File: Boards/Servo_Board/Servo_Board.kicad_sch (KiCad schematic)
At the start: 16 parts, among them U1 STM32G0B1RCTx, U2 ADP2302ARDZ-5.0, Y2 Crystal 8MHz

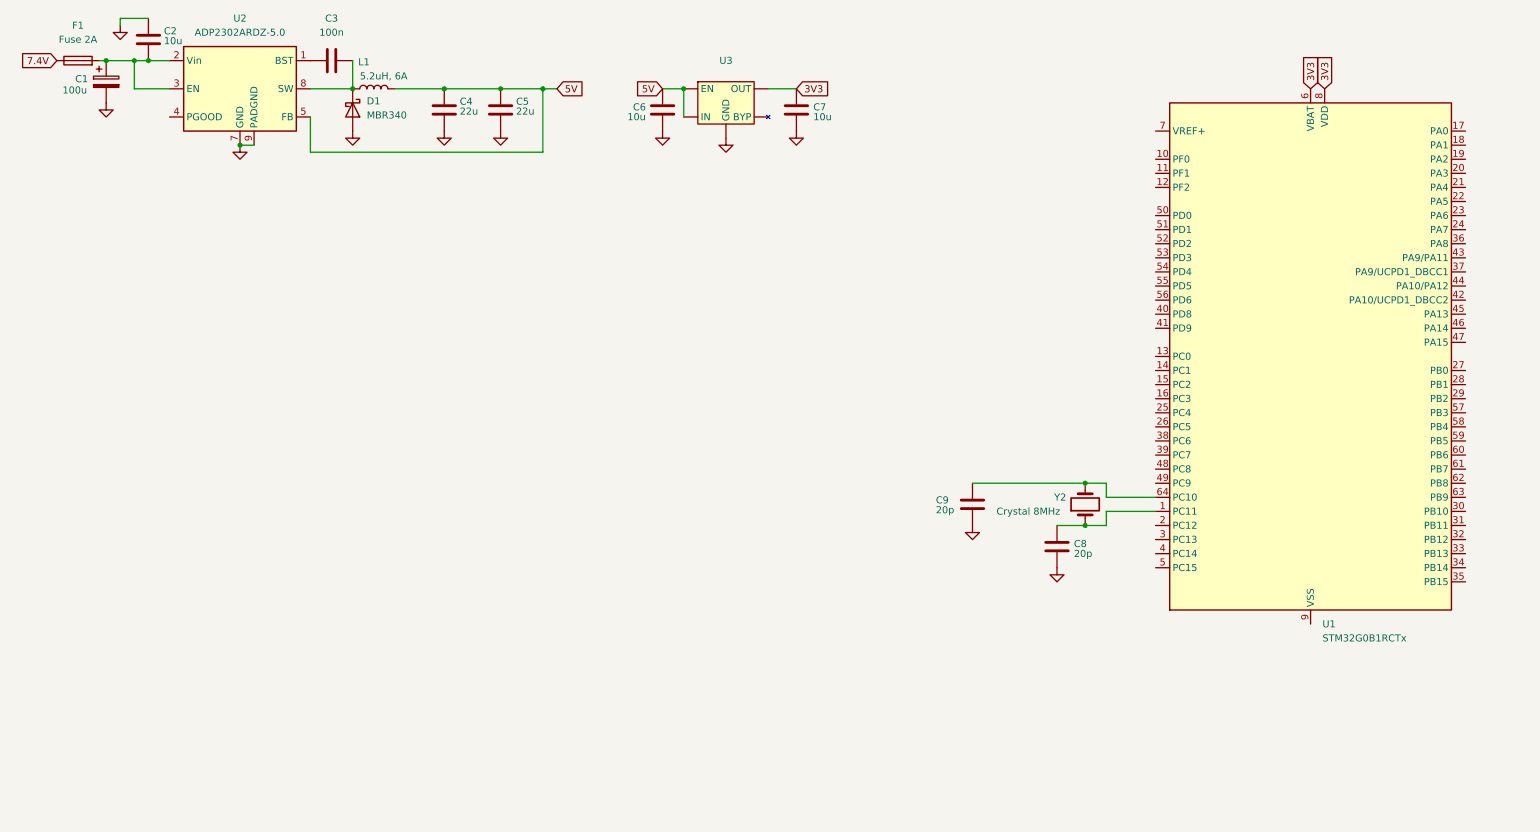
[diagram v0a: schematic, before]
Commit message: CAN transceiver and D-sub connector
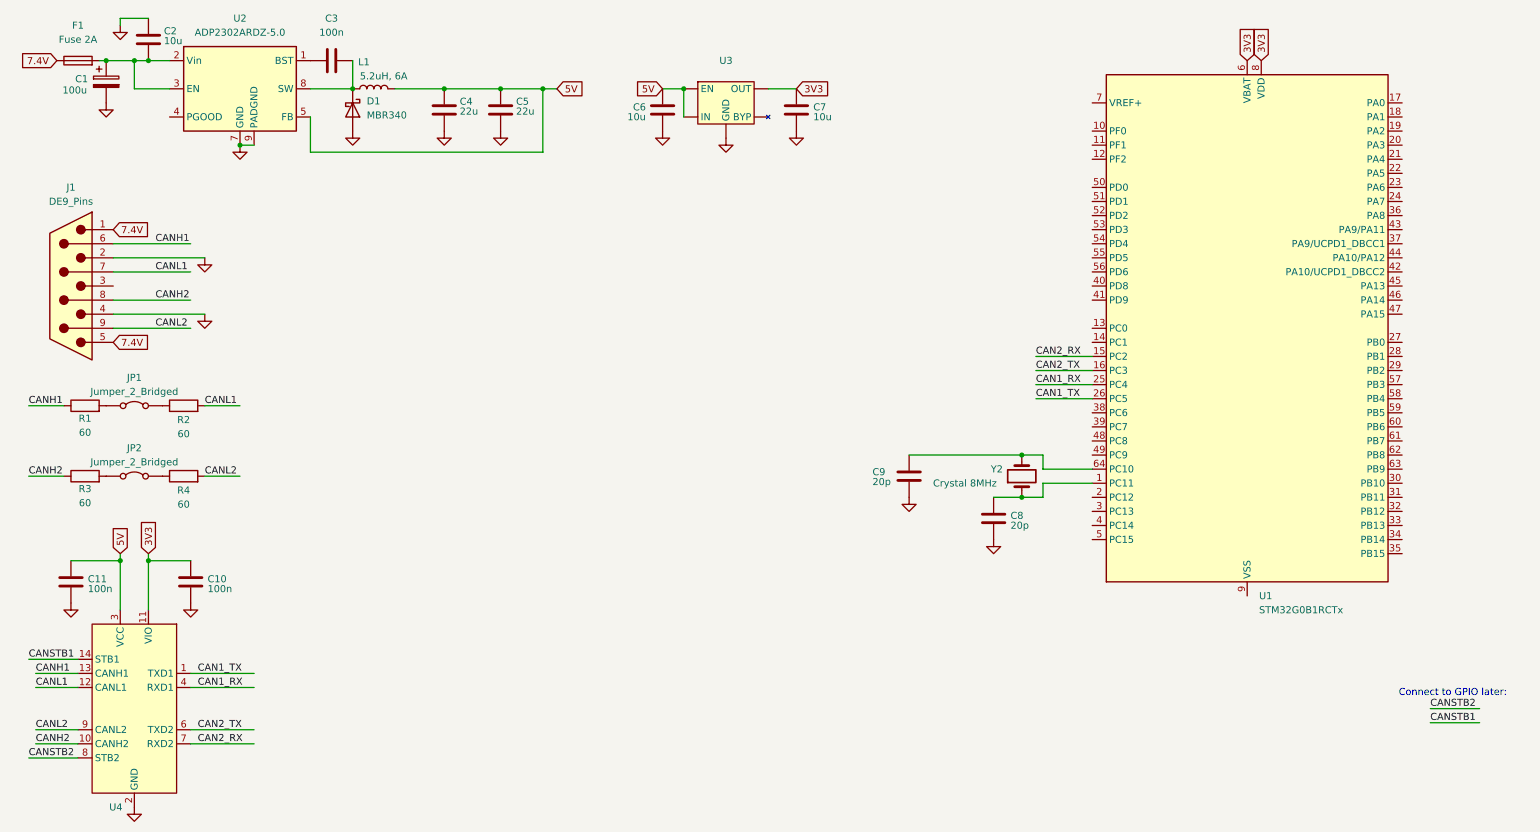
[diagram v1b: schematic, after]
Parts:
- added C10, C11: 100n, symbol Device:C
- added J1: DE9_Pins, symbol Connector:DE9_Pins
- added JP1, JP2: Jumper_2_Bridged, symbol Jumper:Jumper_2_Bridged
- added R1, R2, R3, R4: 60, symbol Device:R
- added U4: ~, Custom:SOT23_DYY_TEX, symbol Interface_CAN_LIN:TCAN1046AV-Q1
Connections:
- net 3V3: now also C10.1, U4.11 (VIO)
- net 5V: now also C11.1, U4.3 (VCC)
- net 7.4V: now also J1.1, J1.5
- net GND: now also C10.2, C11.2, J1.2, J1.4, U4.2 (GND), U4.5 (GND)
- net CAN2_RX: now reaches U1.15 (PC2)
- net CAN2_RX: now also U4.7 (RXD2)
- net CAN2_TX: now reaches U1.16 (PC3)
- net CAN2_TX: now also U4.6 (TXD2)
- net CAN1_RX: now reaches U1.25 (PC4)
- net CAN1_RX: now also U4.4 (RXD1)
- net CAN1_TX: now reaches U1.26 (PC5)
- net CAN1_TX: now also U4.1 (TXD1)
- new net: JP1.1 (A), R1.2
- new net: JP2.2 (B), R4.1
- new net: JP1.2 (B), R2.1
- new net: JP2.1 (A), R3.2
- new net CANH1: J1.6, R1.1, U4.13 (CANH1)
- new net CANH2: J1.8, R3.1, U4.10 (CANH2)
- new net CANL1: J1.7, R2.2, U4.12 (CANL1)
- new net CANL2: J1.9, R4.2, U4.9 (CANL2)
- new net CANSTB1: U4.14 (STB1)
- new net CANSTB2: U4.8 (STB2)
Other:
- note added: "Connect to GPIO later:"
- moved on the sheet: C8, C9, U1, Y2

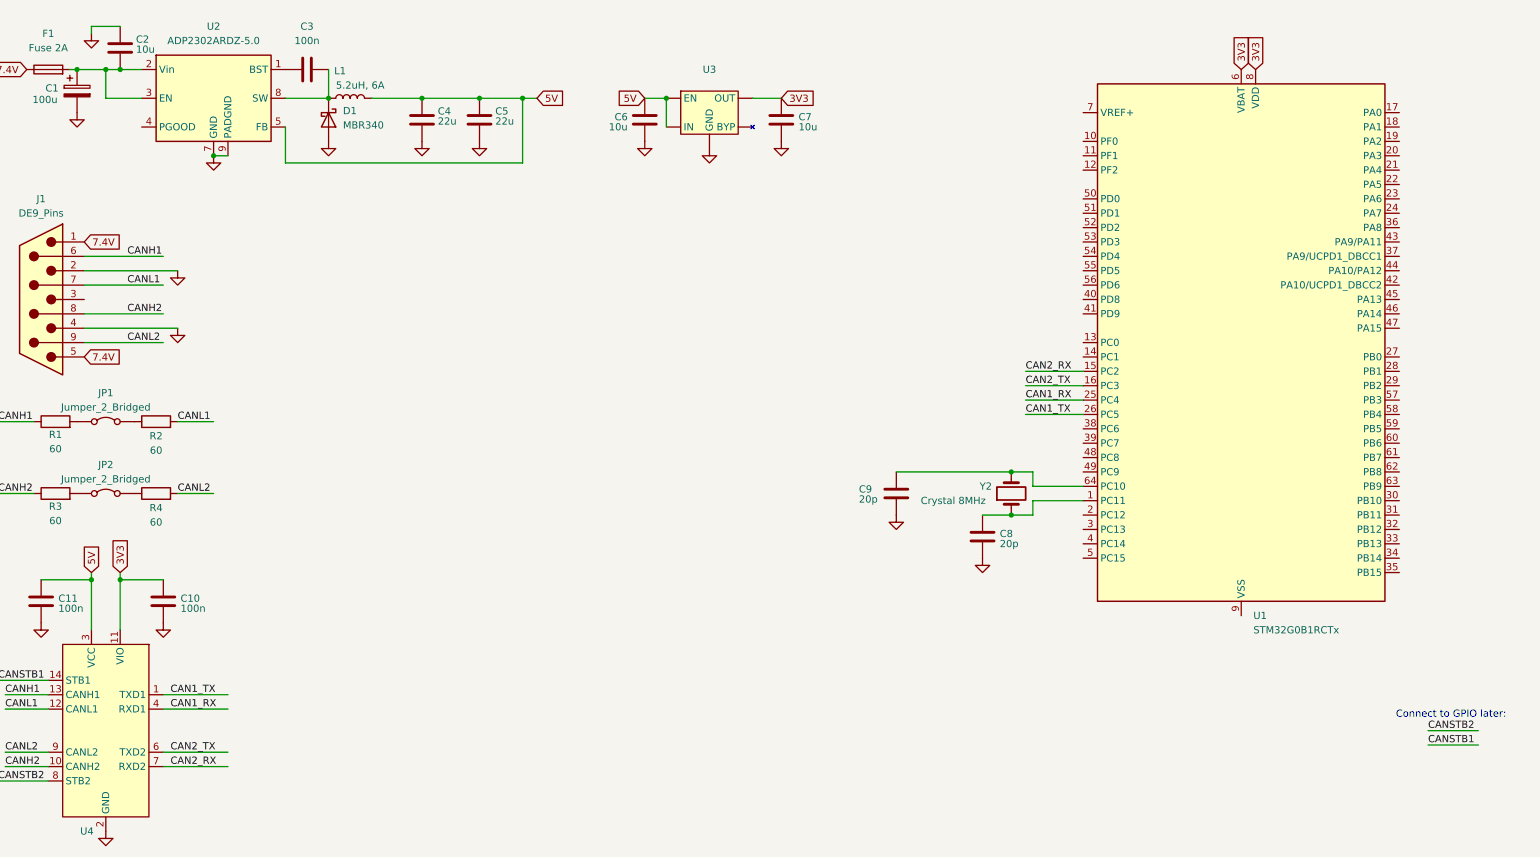
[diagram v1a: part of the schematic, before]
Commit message: Servo board changes:
Replaced buck converter with LDO voltage regulator.
Found PWM pins on u-controller and connected them to connectors with flyback diodes.
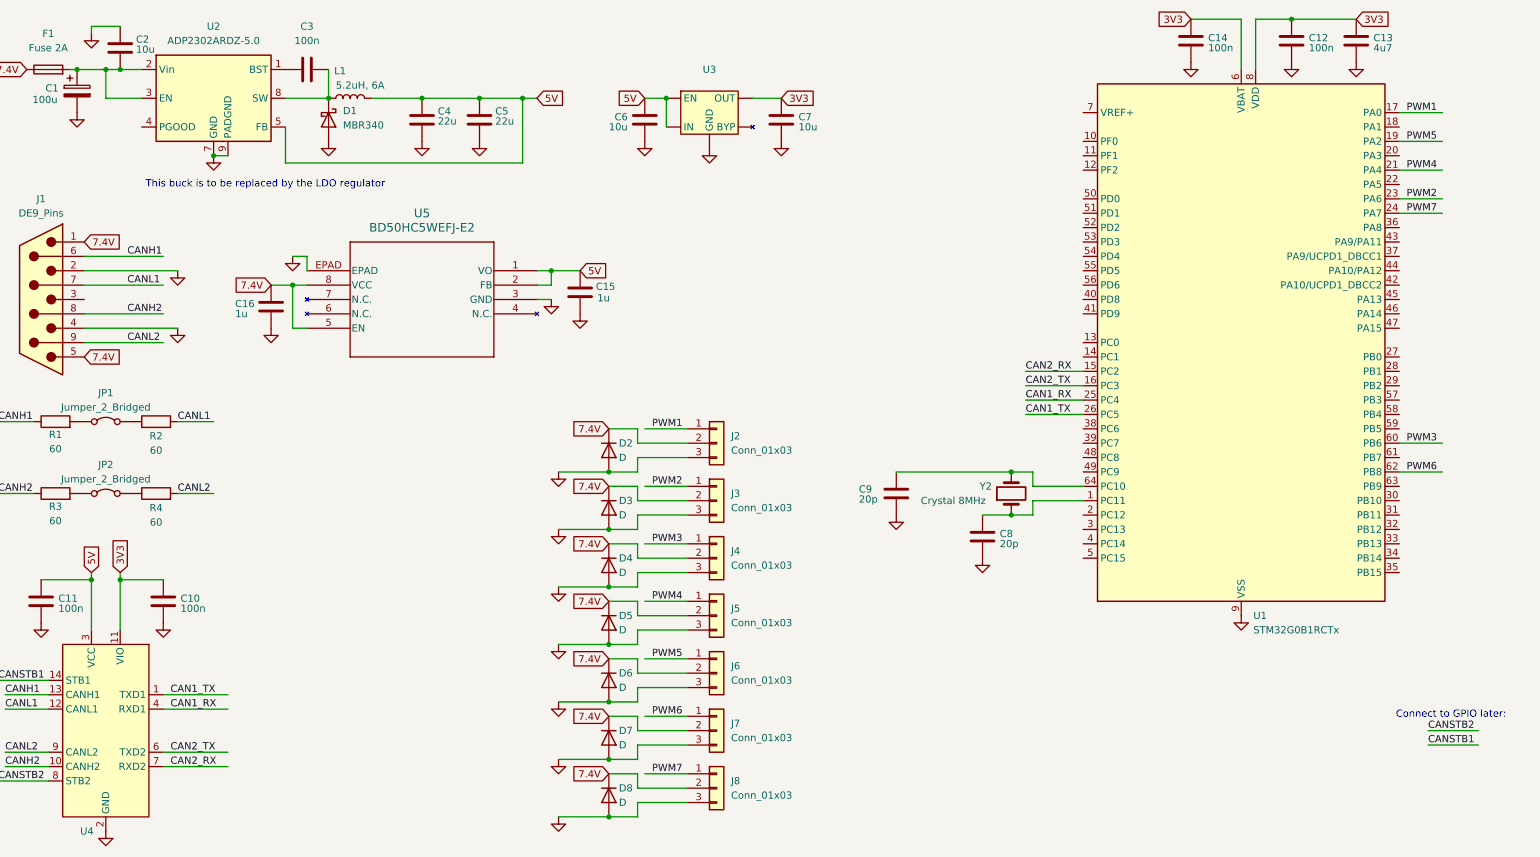
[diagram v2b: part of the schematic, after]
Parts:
- added C12, C14: 100n, symbol Device:C
- added C13: 4u7, symbol Device:C
- added C15, C16: 1u, symbol Device:C
- added D2, D3, D4, D5, D6, D7, D8: D, symbol Device:D
- added J2, J3, J4, J5, J6, J7, J8: Conn_01x03, symbol Connector_Generic:Conn_01x03
- added U5: BD50HC5WEFJ-E2, HTSOP-J8_ROM, symbol 0_Custom_Symbols:BD50HC5WEFJ-E2
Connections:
- net 3V3: now also C12.1, C13.1, C14.1
- net 5V: now also C15.1, U5.1 (VO), U5.2 (FB)
- net 7.4V: now also C16.1, D2.1 (K), D3.1 (K), D4.1 (K), D5.1 (K), D6.1 (K), D7.1 (K), D8.1 (K), J2.2 (Pin_2), J3.2 (Pin_2), J4.2 (Pin_2), J5.2 (Pin_2), J6.2 (Pin_2), J7.2 (Pin_2), J8.2 (Pin_2), U5.5 (EN), U5.8 (VCC)
- net GND: now also U1.9 (VSS), C12.2, C13.2, C14.2, C15.2, C16.2, D2.2 (A), D3.2 (A), D4.2 (A), D5.2 (A), D6.2 (A), D7.2 (A), D8.2 (A), J2.3 (Pin_3), J3.3 (Pin_3), J4.3 (Pin_3), J5.3 (Pin_3), J6.3 (Pin_3), J7.3 (Pin_3), J8.3 (Pin_3), U5.3 (GND), U5.EPAD
- net PWM1: now reaches U1.17 (PA0)
- net PWM1: now also J2.1 (Pin_1)
- net PWM5: now reaches U1.19 (PA2)
- net PWM5: now also J6.1 (Pin_1)
- net PWM4: now reaches U1.21 (PA4)
- net PWM4: now also J5.1 (Pin_1)
- net PWM2: now reaches U1.23 (PA6)
- net PWM2: now also J3.1 (Pin_1)
- net PWM7: now reaches U1.24 (PA7)
- net PWM7: now also J8.1 (Pin_1)
- net PWM3: now reaches U1.60 (PB6)
- net PWM3: now also J4.1 (Pin_1)
- net PWM6: now reaches U1.62 (PB8)
- net PWM6: now also J7.1 (Pin_1)
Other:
- note added: "This buck is to be replaced by the LDO regulator"

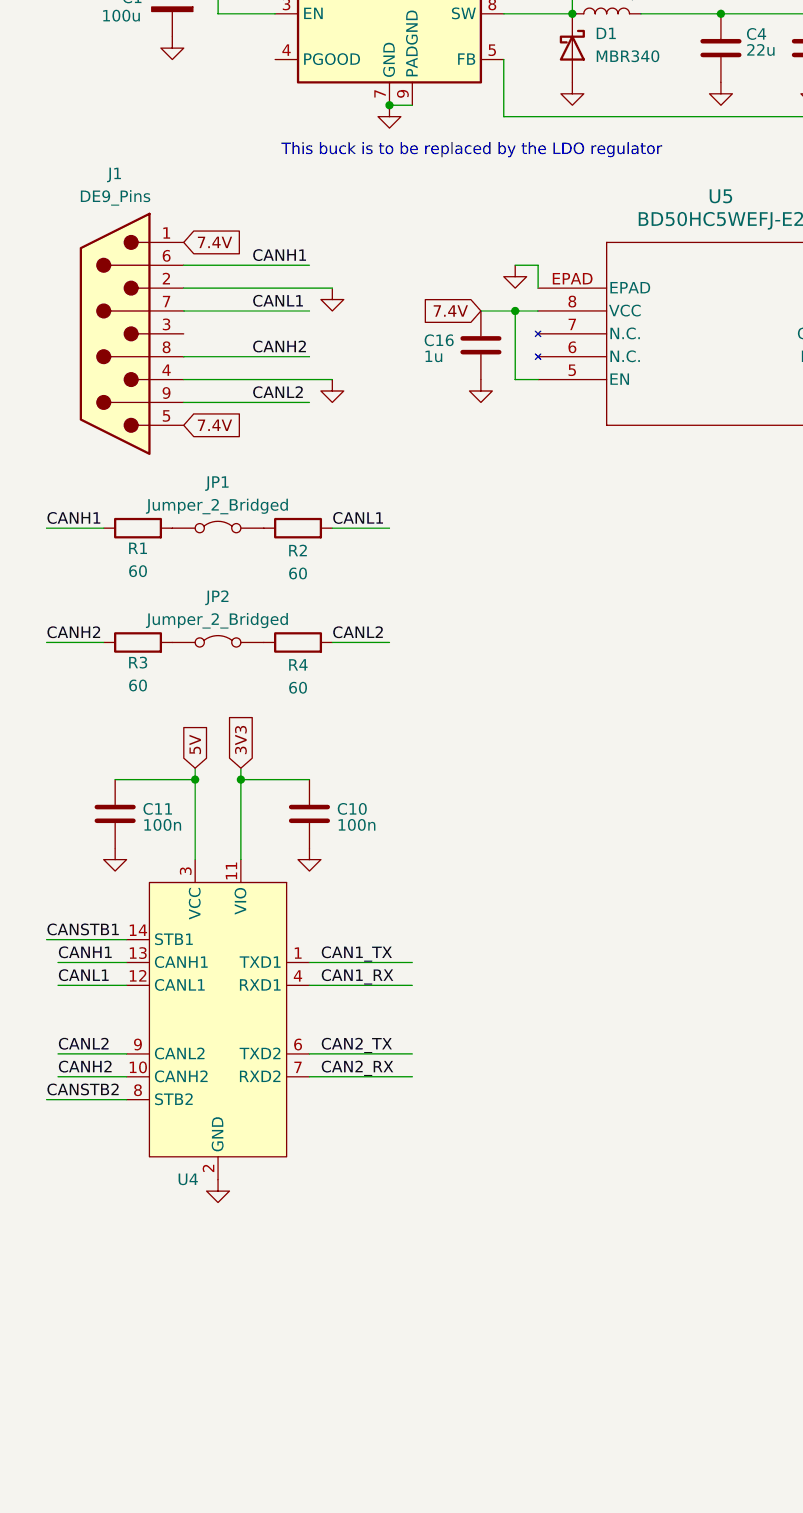
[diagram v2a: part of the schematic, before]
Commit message: D-sub output connector added to servo board
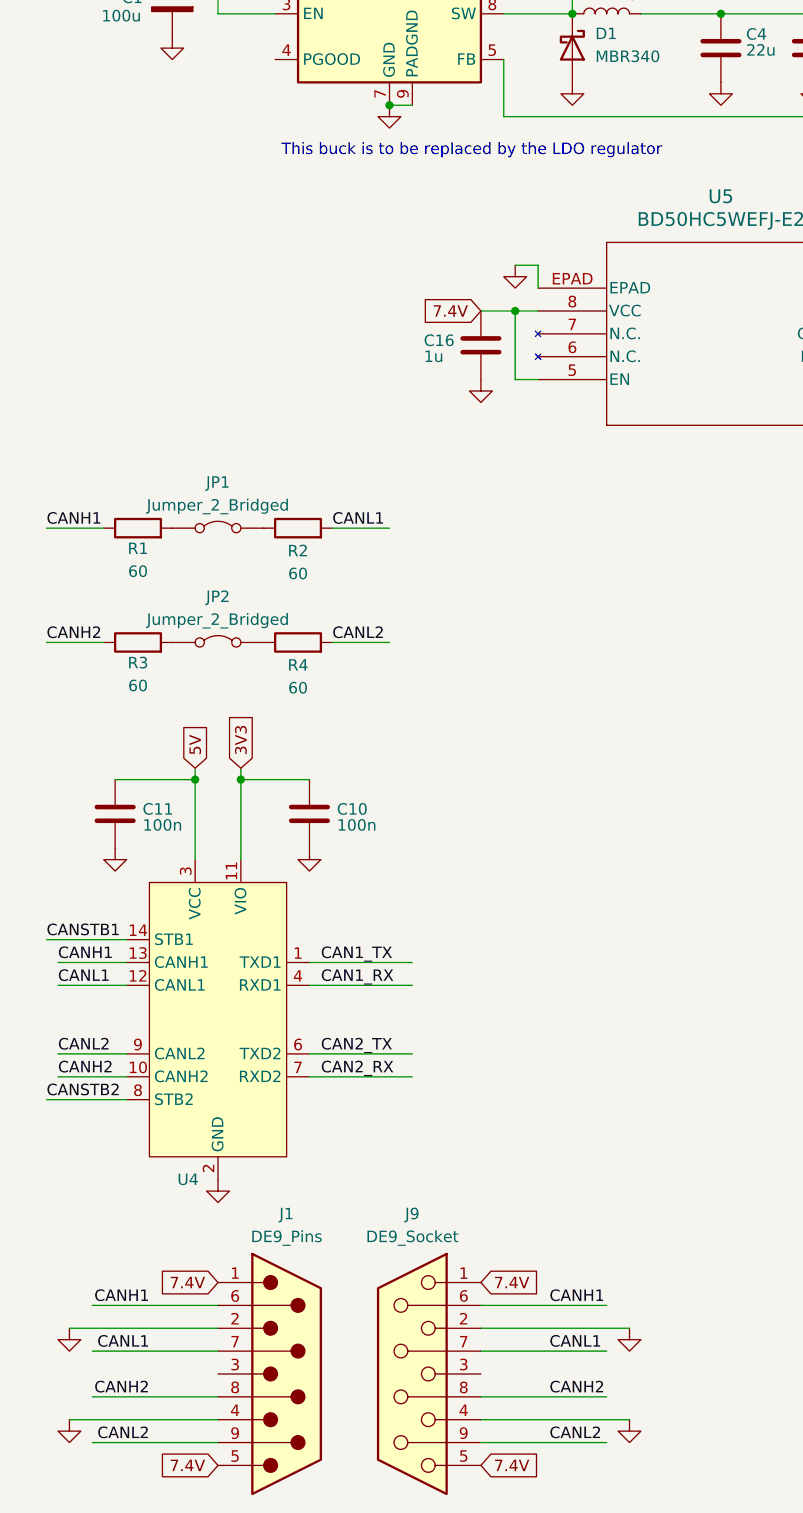
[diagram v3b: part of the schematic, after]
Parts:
- added J9: DE9_Socket, symbol Connector:DE9_Socket
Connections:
- net 7.4V: now also J9.1, J9.5
- net CANH1: now also J9.6
- net CANH2: now also J9.8
- net CANL1: now also J9.7
- net CANL2: now also J9.9
- net GND: now also J9.2, J9.4
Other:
- moved on the sheet: J1
